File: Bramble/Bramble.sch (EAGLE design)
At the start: 17 parts

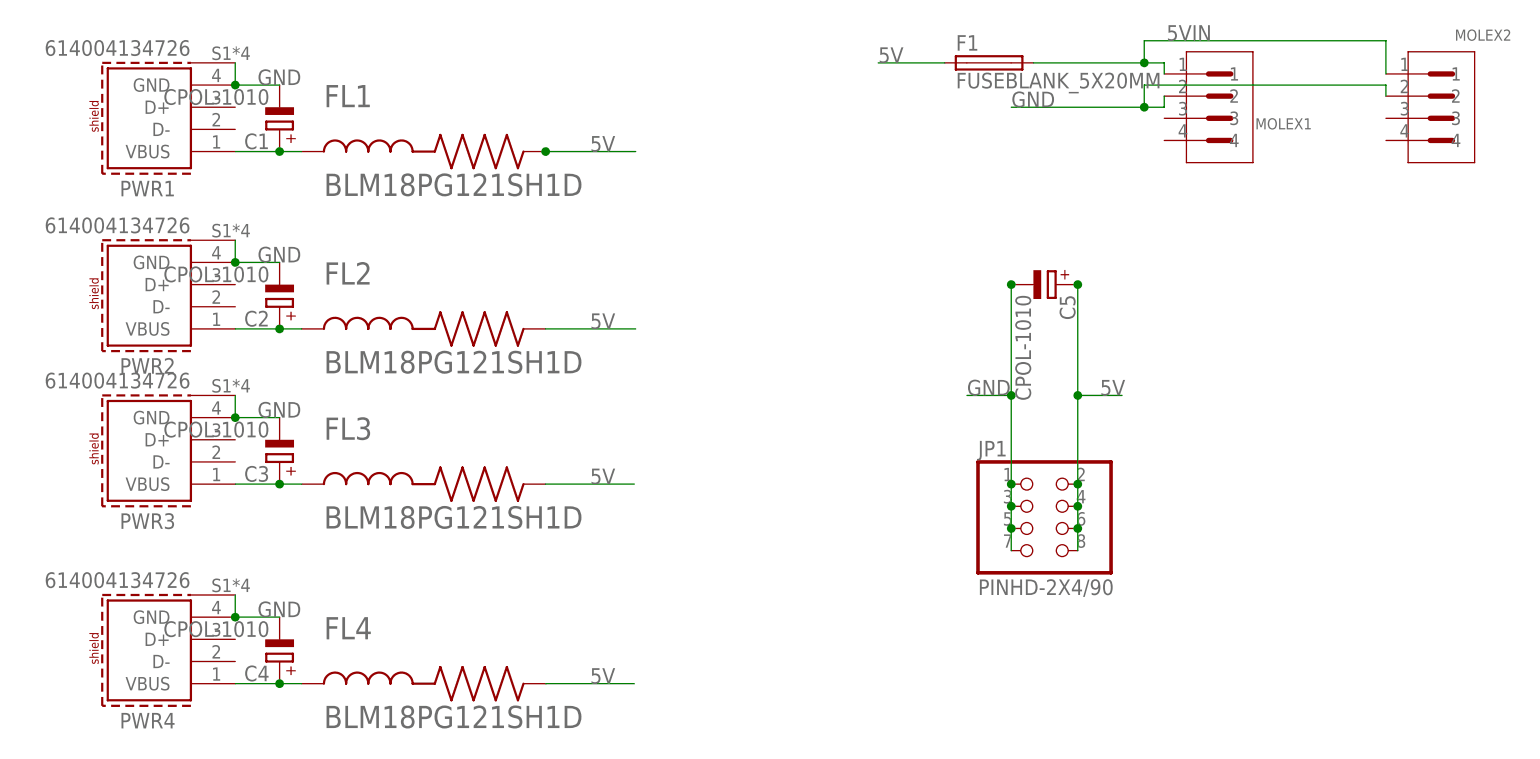
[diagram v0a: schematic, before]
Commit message: Updated ferite bead value
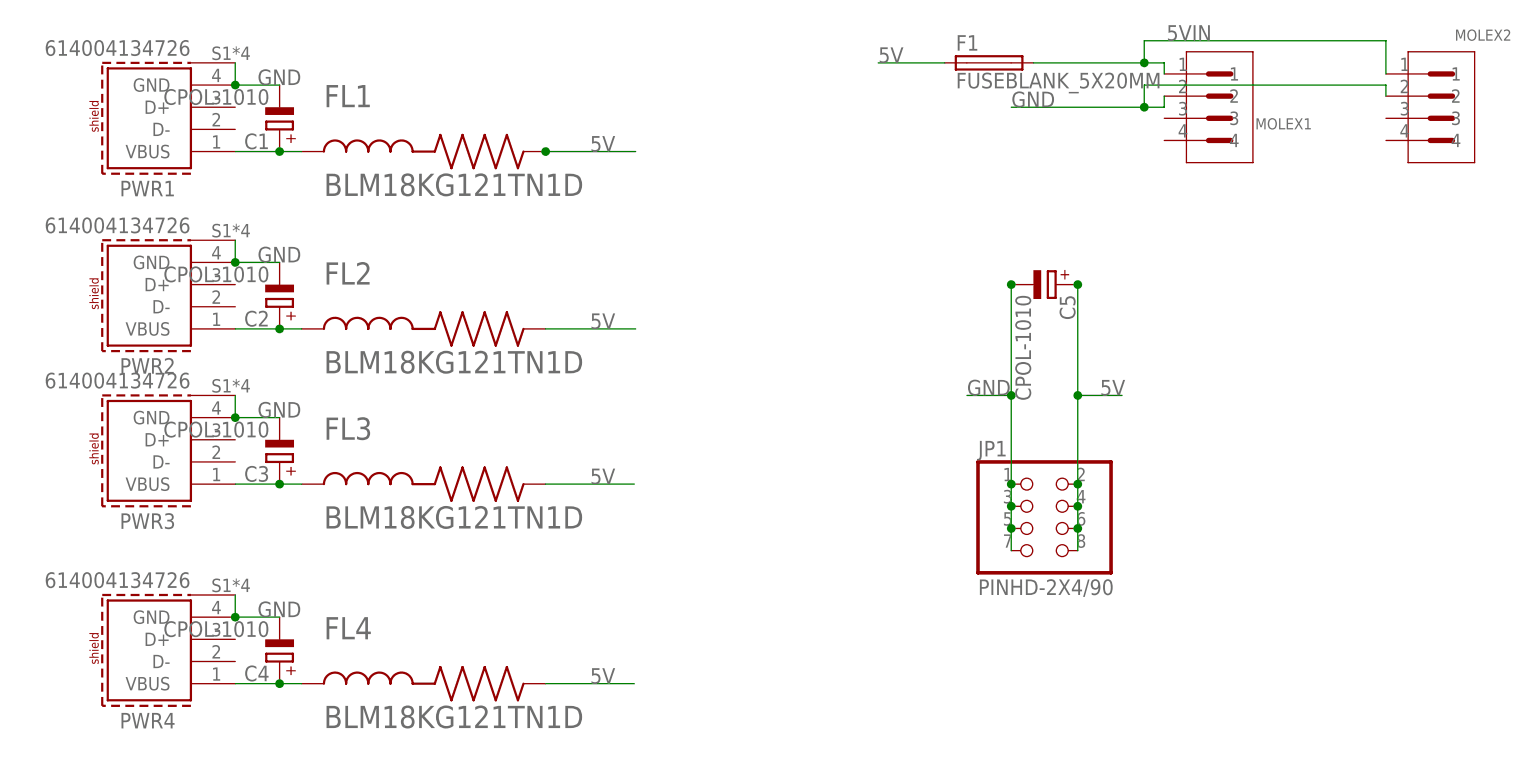
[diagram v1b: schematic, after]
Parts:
- FL1, FL2, FL3, FL4: value BLM18PG121SH1D -> BLM18KG121TN1D
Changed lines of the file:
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@@
 <part name="C4" library="cap-vishay-153clv" deviceset="CPOL-1010" device=""/>
 <part name="C5" library="cap-vishay-153clv" deviceset="CPOL-1010" device=""/>
-<part name="FL1" library="BLM18PG121SH1D" deviceset="BLM18PG121SH1D" device=""/>
-<part name="FL2" library="BLM18PG121SH1D" deviceset="BLM18PG121SH1D" device=""/>
-<part name="FL3" library="BLM18PG121SH1D" deviceset="BLM18PG121SH1D" device=""/>
-<part name="FL4" library="BLM18PG121SH1D" deviceset="BLM18PG121SH1D" device=""/>
+<part name="FL1" library="BLM18PG121SH1D" deviceset="BLM18PG121SH1D" device="" value="BLM18KG121TN1D"/>
+<part name="FL2" library="BLM18PG121SH1D" deviceset="BLM18PG121SH1D" device="" value="BLM18KG121TN1D"/>
+<part name="FL3" library="BLM18PG121SH1D" deviceset="BLM18PG121SH1D" device="" value="BLM18KG121TN1D"/>
+<part name="FL4" library="BLM18PG121SH1D" deviceset="BLM18PG121SH1D" device="" value="BLM18KG121TN1D"/>
 <part name="MOLEX1" library="15244441" deviceset="15244441" device=""/>
 <part name="MOLEX2" library="15244441" deviceset="15244441" device=""/>
